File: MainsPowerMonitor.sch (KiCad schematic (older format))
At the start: 11 parts, among them J401 Screw_Terminal_01x02, J402 AudioJack2_SwitchT

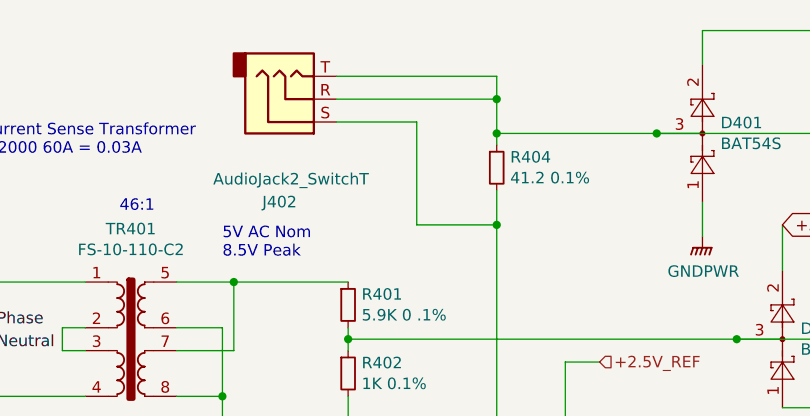
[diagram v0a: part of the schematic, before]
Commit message: Replaced the 3.5mm headphone jack which was used as the current transformer input, I thought due to the dangerous voltages that can be developed if it is connected to the mains without being pluged into the burden resistor located on the board, that it might be better to cut the connector off an wire it to the board, this would also allow for the option of perhapes a 10V zener to be solder accross the outputs of the current sense transformer.
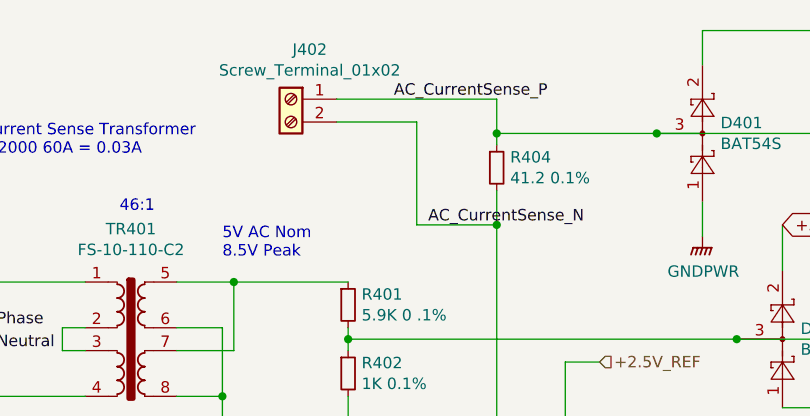
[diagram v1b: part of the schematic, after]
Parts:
- removed J402: AudioJack2_SwitchT, Connect_jl:Audio_StereoJack_3.5mm_ASJ-99H-R-HT-T, symbol Connector:AudioJack3
- added J402: Screw_Terminal_01x02, digikey-footprints:Term_Block_1x2_P5mm, symbol Connector:Screw_Terminal_01x02
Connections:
- net Mains_Current: now also J402.1 (Pin_1)
- net AC_CurrentSense_N: now reaches C401.1, R402.2, R404.2, R405.2, R406.1, TR401.6, TR401.8
- net AC_CurrentSense_N: now also J402.2 (Pin_2)
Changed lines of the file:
@@
-$EndComp
-$Comp
-L Connector:AudioJack3 J402
-U 1 1 5F18094B
-P 3400 2900
-F 0 "J402" H 3350 3350 50  0000 C CNN
-F 1 "AudioJack2_SwitchT" H 3400 3250 50  0000 C CNN
-F 2 "Connect_jl:Audio_StereoJack_3.5mm_ASJ-99H-R-HT-T" H 3400 2900 50  0001 C CNN
-F 3 "http://www.adam-tech.com/downloader.php?p=ASJ-99H-X-HT-TR.pdf" H 3400 2900 50  0001 C CNN
-F 4 "Adam Tech" H 0   0   50  0001 C CNN "MFR"
-F 5 "ASJ-99H-R-HT-T/R" H 0   0   50  0001 C CNN "MPN"
-F 6 "digikey" H 0   0   50  0001 C CNN "SPR"
-F 7 "2057-ASJ-99H-R-HT-T/RCT-ND" H 0   0   50  0001 C CNN "SPN"
-F 8 "-" H 0   0   50  0001 C CNN "SPURL"
-	1    3400 2900
-	1    0    0    1
 $EndComp
 $Comp
@@
 	4300 3450 4300 4600
 Wire Wire Line
-	3600 2800 4300 2800
-Wire Wire Line
-	4300 2800 4300 2900
-Wire Wire Line
 	3600 2900 4300 2900
 Wire Wire Line
@@
 Connection ~ 4300 3450
 Connection ~ 4300 3050
-Connection ~ 4300 2900
 Text Notes 5150 4850 0    50   ~ 0
 Note R405 and R406 put 1.25mA\nLoad on ultimately on the 3.0V supply\nwhich is used to privide input protection\nto the micro.  Without the load the \nvoltage would just rise.
+$Comp
+L Connector:Screw_Terminal_01x02 J402
+U 1 1 5F7AFA6B
+P 3400 2900
+F 0 "J402" H 3318 3117 50  0000 C CNN
+F 1 "Screw_Terminal_01x02" H 3318 3026 50  0000 C CNN
+F 2 "digikey-footprints:Term_Block_1x2_P5mm" H 3400 2900 50  0001 C CNN
+F 3 "https://media.digikey.com/pdf/Data%20Sheets/Phoenix%20Contact%20PDFs/1792863.pdf" H 3400 2900 50  0001 C CNN
+F 4 "Phoenix Contact" H 1900 -1000 50  0001 C CNN "MFR"
+F 5 "1792863" H 1900 -1000 50  0001 C CNN "MPN"
+F 6 "digikey" H 1900 -1000 50  0001 C CNN "SPR"
+F 7 "277-2518-ND" H 1900 -1000 50  0001 C CNN "SPN"
+F 8 "-" H 1900 -1000 50  0001 C CNN "SPURL"
+	1    3400 2900
+	-1   0    0    -1
+$EndComp
+Text Label 3850 2900 0    50   ~ 0
+AC_CurrentSense_P
+Text Label 4000 3450 0    50   ~ 0
+AC_CurrentSense_N
 $EndSCHEMATC

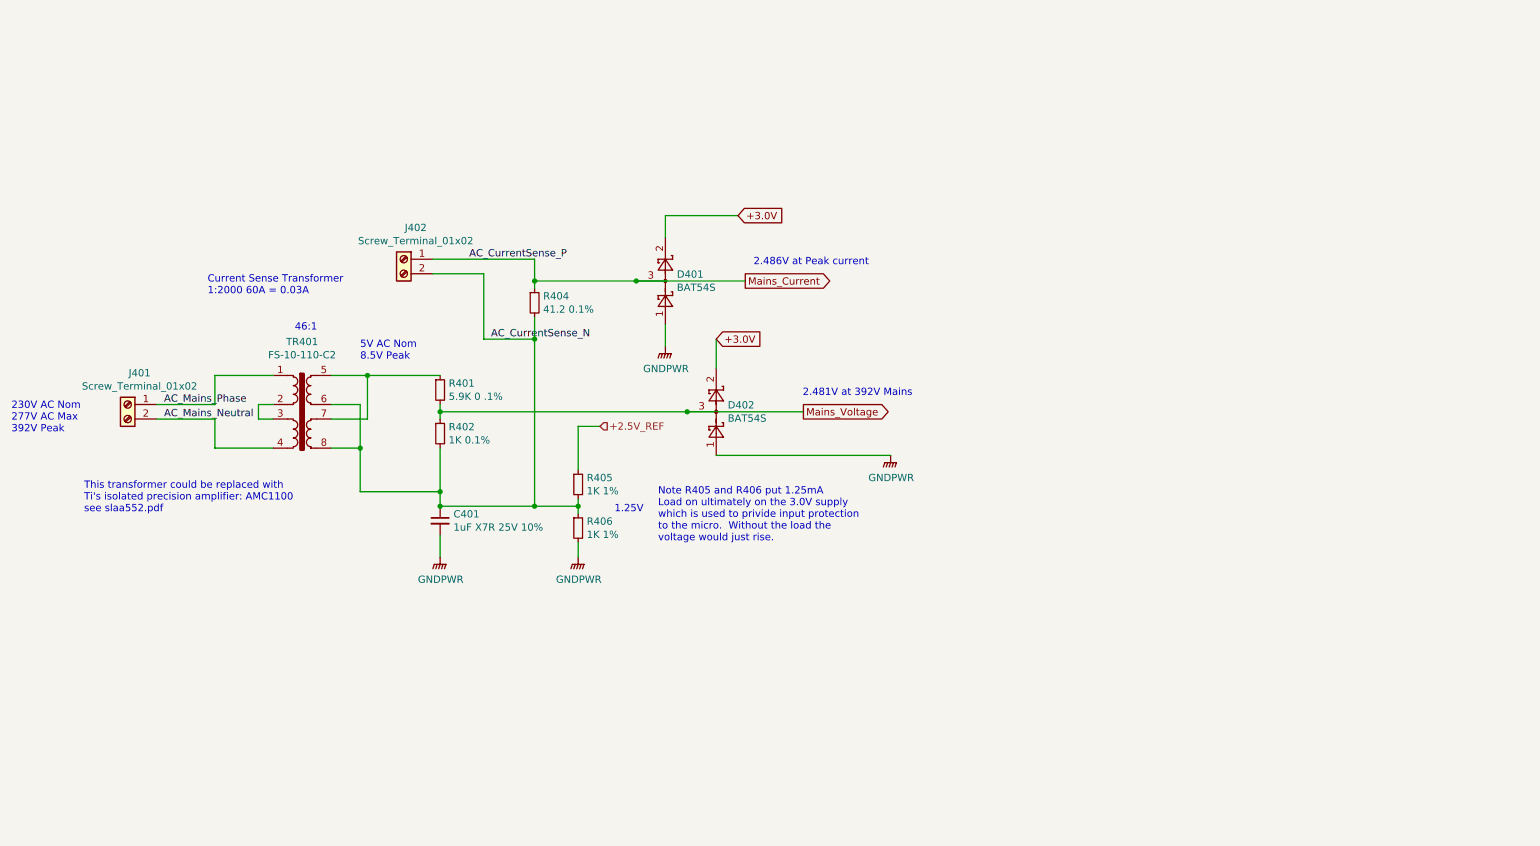
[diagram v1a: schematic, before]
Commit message: Added Auto Range circuit to the Mains Current Sense, this will give close to 1W resolution on the mains measurment in the range 0-2000W vs about 6.6W resolution.  Updated the BOM, which I think caused a heap of files to appear changed to git.  Also spotted an error on the 41.2 ohm resistor , had a digikey partnumber of a 41.2K ohm part, which would have probable smoked something at that been inserted in the path of a current source shuch as the current transformer.
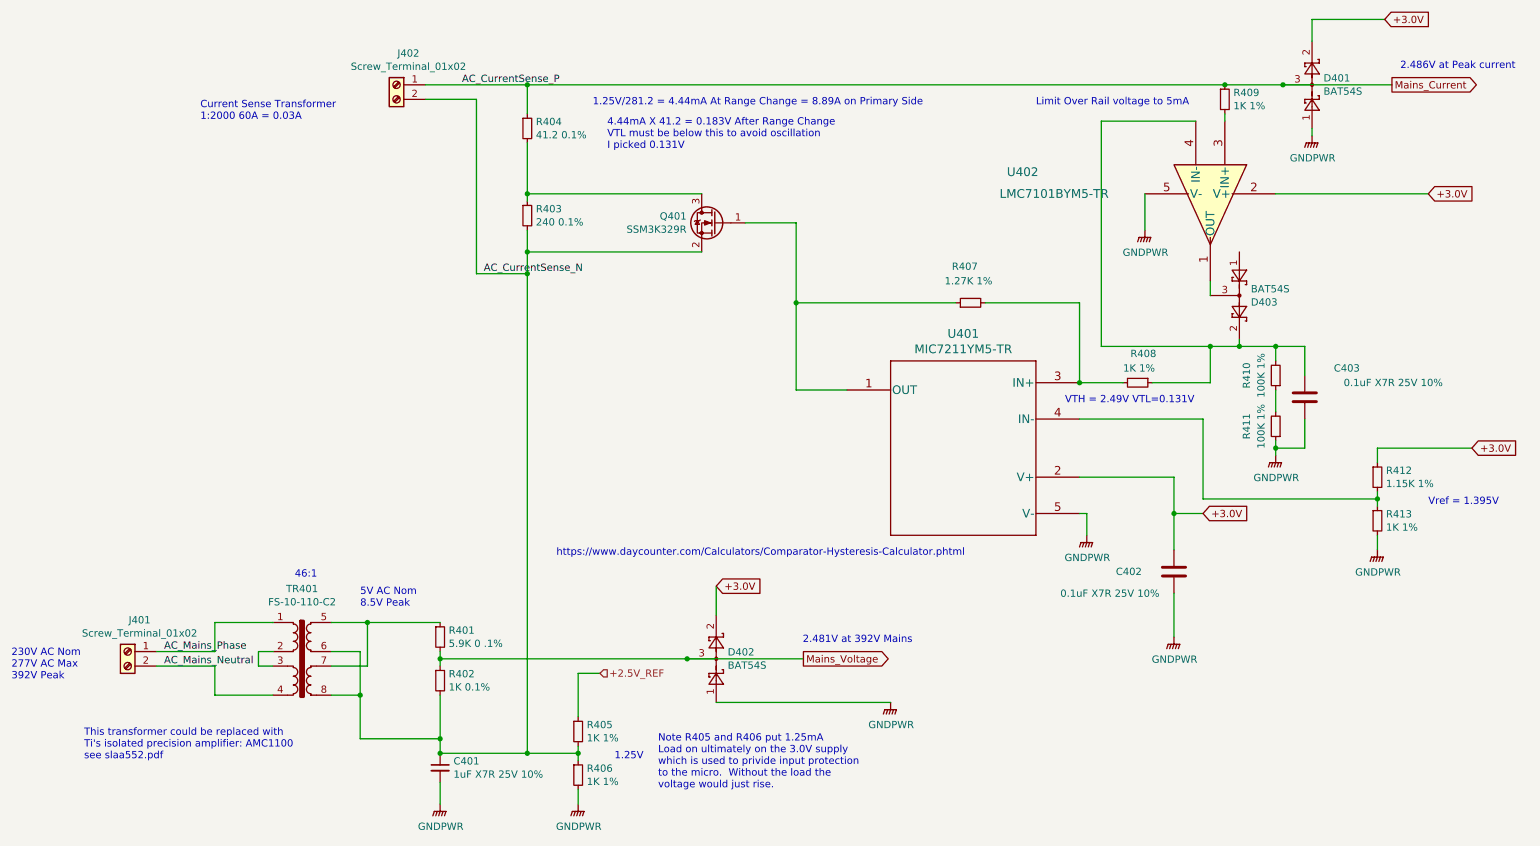
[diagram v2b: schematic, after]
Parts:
- added C402, C403: 0.1uF X7R 25V 10%, Capacitor_SMD:C_0805_2012Metric_Pad1.15x1.40mm_HandSolder, symbol Device:C
- added D403: BAT54S, Package_TO_SOT_SMD:SOT-23_Handsoldering, symbol Diode:BAT54S
- added Q401: SSM3K329R, Package_TO_SOT_SMD:SOT-23_Handsoldering, symbol Device:Q_NMOS_GSD
- added R403: 240 0.1%, Resistor_SMD:R_0805_2012Metric_Pad1.15x1.40mm_HandSolder, symbol Device:R_Small
- added R407: 1.27K 1%, Resistor_SMD:R_0805_2012Metric_Pad1.15x1.40mm_HandSolder, symbol Device:R_Small
- added R408, R409, R413: 1K 1%, Resistor_SMD:R_0805_2012Metric_Pad1.15x1.40mm_HandSolder, symbol Device:R_Small
- added R410, R411: 100K 1%, Resistor_SMD:R_0805_2012Metric_Pad1.15x1.40mm_HandSolder, symbol Device:R_Small
- added R412: 1.15K 1%, Resistor_SMD:R_0805_2012Metric_Pad1.15x1.40mm_HandSolder, symbol Device:R_Small
- added U401: MIC7211YM5-TR, Package_TO_SOT_SMD:SOT-23-5_HandSoldering, symbol MicroChip:MIC7211YM5-TR
- added U402: LMC7101BYM5-TR, Package_TO_SOT_SMD:SOT-23-5_HandSoldering, symbol MicroChip:LMC7101BYM5-TR
- R404: MFR Panasonic Electronic Components -> TE Connectivity Passive Product; MPN ERA-6AEB4122V -> 8-1625868-6; SPN P41.2KDACT-ND -> A110410CT-ND
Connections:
- net +3.0V: now also C402.1, R412.1, U401.2 (V+), U402.2 (V+)
- net AC_CurrentSense_N: now also Q401.2 (S), R403.2; no longer R404.2
- net GNDPWR: now also C402.2, C403.2, R411.1, R413.2, U401.5 (V-), U402.5 (V-)
- net Mains_Current: now also R409.1
- new net: Q401.3 (D), R403.1, R404.2
- new net: Q401.1 (G), R407.1, U401.1 (OUT)
- new net: R407.2, R408.2, U401.3 (IN+)
- new net: R412.2, R413.1, U401.4 (IN-)
- new net: C403.1, D403.2, R408.1, R410.2, U402.4 (IN-)
- new net: D403.3, U402.1 (OUT)
- new net: R410.1, R411.2
- new net: R409.2, U402.3 (IN+)
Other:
- note added: "1.25V/281.2 = 4.44mA At Range Change = 8.89A on Primary Side"
- note added: "4.44mA X 41.2 = 0.183V After Range Change\nVTL must be below this to avoid oscillation\nI picked 0.131V"
- note added: "Limit Over Rail voltage to 5mA"
- note added: "VTH = 2.49V VTL=0.131V"
- note added: "Vref = 1.395V"
- note added: "https://www.daycounter.com/Calculators/Comparator-Hysteresis-Calculator.phtml"
- moved on the sheet: C401, D401, D402, J401, J402, R401, R402, R404, R405, R406, TR401

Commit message: Added Current_Range_Hi_Lo signal from the Mains Current Sense circuit to the Micro so we can tell what range we are operating on.
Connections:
- net Current_Range_Hi_Lo: now reaches Q401.1 (G), R407.1, U401.1 (OUT)
